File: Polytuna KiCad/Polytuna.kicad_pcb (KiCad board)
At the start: 2 copper layers, 114.3 x 64.8 mm, 47 parts, among them IC1 AP7313-33SAG-7, J1 Barrel_Jack, J2 Conn_01x02, J3 Conn_01x02, J4 Conn_01x04, J5 Conn_01x02, SW1 SW_Push, SW2 SW_Push, SW3 SW_Push, SW4 SW_TPDT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

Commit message: Added some logos
Still in need of tunas
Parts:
- G***: footprint uc3music_logos:logo_guitar_45x15.4mm -> uc3music_logos:logo_guitar_52.6.5x18.4mm
- moved G*** 4.35 mm to (156.5, 89.2)
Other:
- board text added: "Sergio Sánchez Rodríguez"

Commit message: Moar logos
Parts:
- moved J2 2.54 mm to (161.3, 142.2), turned to 270 degrees
- moved J3 2.54 mm to (174.2, 142.2), turned to 270 degrees
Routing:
- net GND: track 160.0 -> 193.4 mm
- net GNDA: track 39.2 -> 64.4 mm
- net Pin11_Teensy: track 11.4 -> 12.1 mm
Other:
- board text added: "Battery"

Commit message: Changed some logos. Added a tuna
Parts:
- removed the G*** at (218.8, 120.9)
- added G***: LOGO, uc3music_logos:logo_pick_10x10mm, F.Cu at (162.8, 111.8)
- added G***: LOGO, Silks Polytuna:tuna_fish_logo_21.7x21.7mm, F.Cu at (221.7, 120.1)

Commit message: MOAR TUNAS FOR EVERYBODY
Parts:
- added G***: LOGO, Silks Polytuna:tuna_fish_back1_L_54.2x27.1mm, B.Cu at (193.0, 71.1)
- added G***: LOGO, Silks Polytuna:tuna_fish_back3_R_8.1x8.1mm, B.Cu at (159.5, 102.6)
- added G***: LOGO, Silks Polytuna:tuna_fish_logo_10.8x10.8mm, B.Cu at (195.6, 126.0)
- added G***: LOGO, Silks Polytuna:tuna_fish_back3_L_19x9.5mm, B.Cu at (134.6, 103.4)
- added G***: LOGO, Silks Polytuna:tuna_fish_back1_L_25x12.5mm, B.Cu at (224.0, 129.0)
- added G***: LOGO, Silks Polytuna:tuna_fish_back2_R_16.4x16.4mm, B.Cu at (148.8, 133.1)
- added G***: LOGO, Silks Polytuna:tuna_fish_back3_R_15.5x7.7mm, B.Cu at (210.3, 117.1)
- added G***: LOGO, Silks Polytuna:tuna_fish_back1_L_8.1x4.1mm, F.Cu at (133.9, 136.9)
- moved Output1 0.80 mm to (193.3, 91.2)

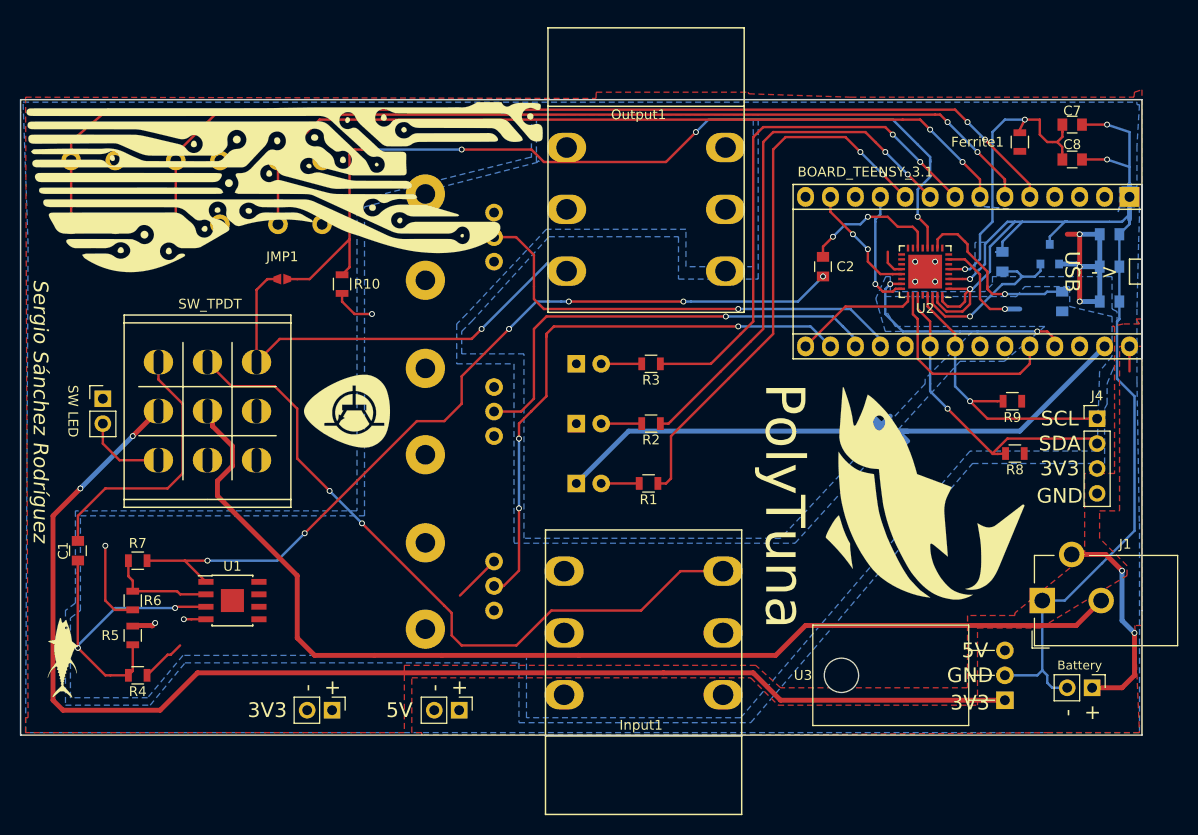
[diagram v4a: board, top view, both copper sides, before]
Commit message: Added some "Pibbles" and no DRC errors
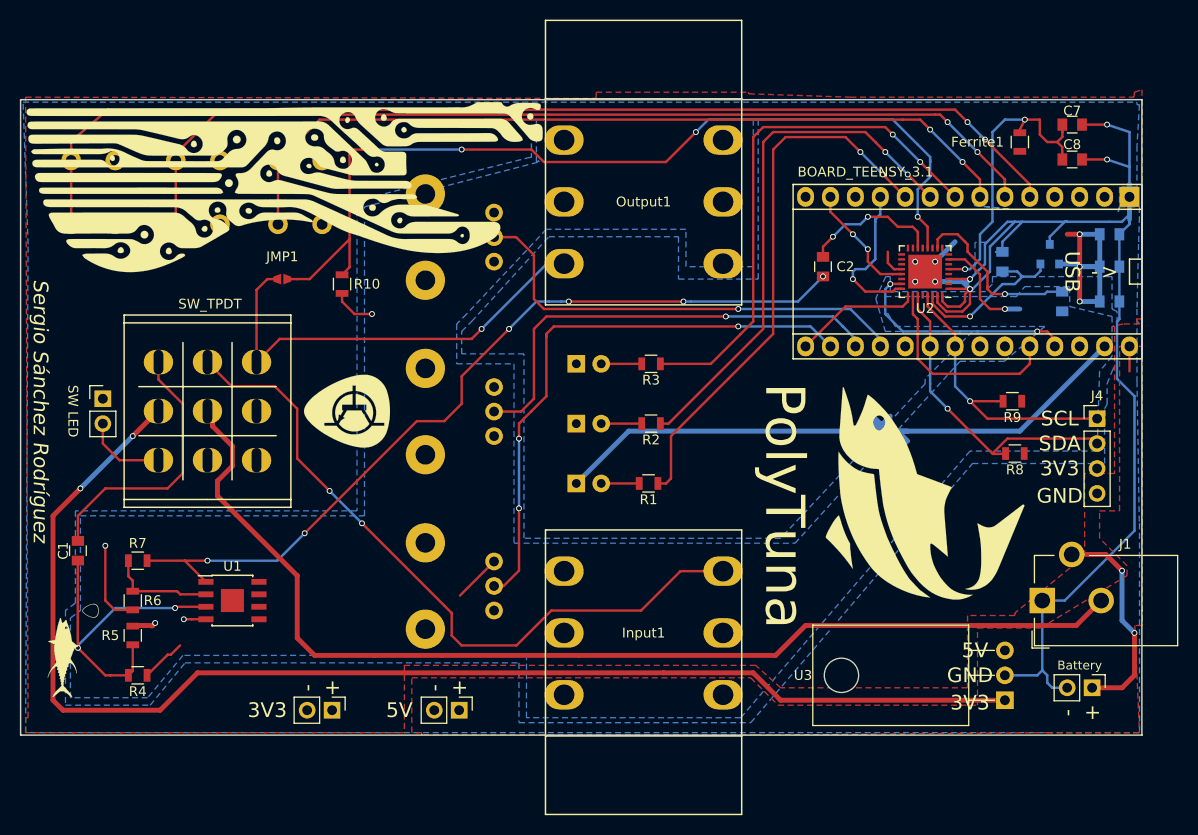
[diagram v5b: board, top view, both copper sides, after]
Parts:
- added G***: LOGO, Silks Polytuna:pick_contour_1.7mm, B.Cu at (135.6, 114.3)
- added G***: LOGO, Silks Polytuna:pick_contour_3mm, B.Cu at (141.2, 114.3)
- added G***: LOGO, Silks Polytuna:pick_contour_3mm, B.Cu at (152.4, 123.7)
- added G***: LOGO, Silks Polytuna:pick_contour_1.7mm, B.Cu at (157.5, 125.5)
- added G***: LOGO, Silks Polytuna:pick_contour_3.4mm, B.Cu at (197.9, 100.6)
- added G***: LOGO, Silks Polytuna:pick_contour_2.7mm, B.Cu at (205.5, 99.3)
- added G***: LOGO, Silks Polytuna:pick_contour_1.7mm, B.Cu at (210.1, 101.9)
- added G***: LOGO, Silks Polytuna:pick_contour_1.7mm, B.Cu at (162.3, 97.0)
- added G***: LOGO, Silks Polytuna:pick_contour_1.7mm, B.Cu at (195.3, 132.3)
- added G***: LOGO, Silks Polytuna:pick_contour_2.7mm, B.Cu at (200.2, 131.1)
- added G***: LOGO, Silks Polytuna:pick_contour_2.7mm, B.Cu at (213.9, 108.7)
- added G***: LOGO, Silks Polytuna:pick_contour_3.4mm, B.Cu at (232.7, 143.0)
- added G***: LOGO, Silks Polytuna:pick_contour_1.7mm, B.Cu at (223.5, 108.0)
- added G***: LOGO, Silks Polytuna:pick_contour_2.2mm, B.Cu at (219.2, 110.7)
- added G***: LOGO, Silks Polytuna:pick_contour_2.2mm, B.Cu at (162.1, 123.4)
- added G***: LOGO, Silks Polytuna:pick_contour_1.7mm, F.Cu at (136.7, 132.1)
- moved Output1 0.80 mm to (193.0, 90.4)
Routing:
- net GND: track 193.4 -> 203.8 mm
- net Pin9_Teensy: track 12.2 -> 15.7 mm

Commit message: PCB v1 finished
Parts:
- added G***: LOGO, Silks Polytuna:pick_contour_1.7mm, B.Cu at (227.1, 141.7)
- moved JMP2 0.25 mm to (217.9, 114.0), turned to 135 degrees
- renumbered D1 to LED1, D2 to LED2, D3 to LED3
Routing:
- net GNDA: track 64.4 -> 60.7 mm
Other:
- board text added: "A0"
- board text added: "A1"
- board text added: "A2"
- board text added: "D3"
- board text added: "D4"
- board text added: "D5"
- board text added: "D6"
- board text added: "D7"
- board text added: "D8"

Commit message: Some fixes
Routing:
- net GND: track 203.8 -> 209.7 mm
- net +3V3: track 50.2 -> 45.6 mm

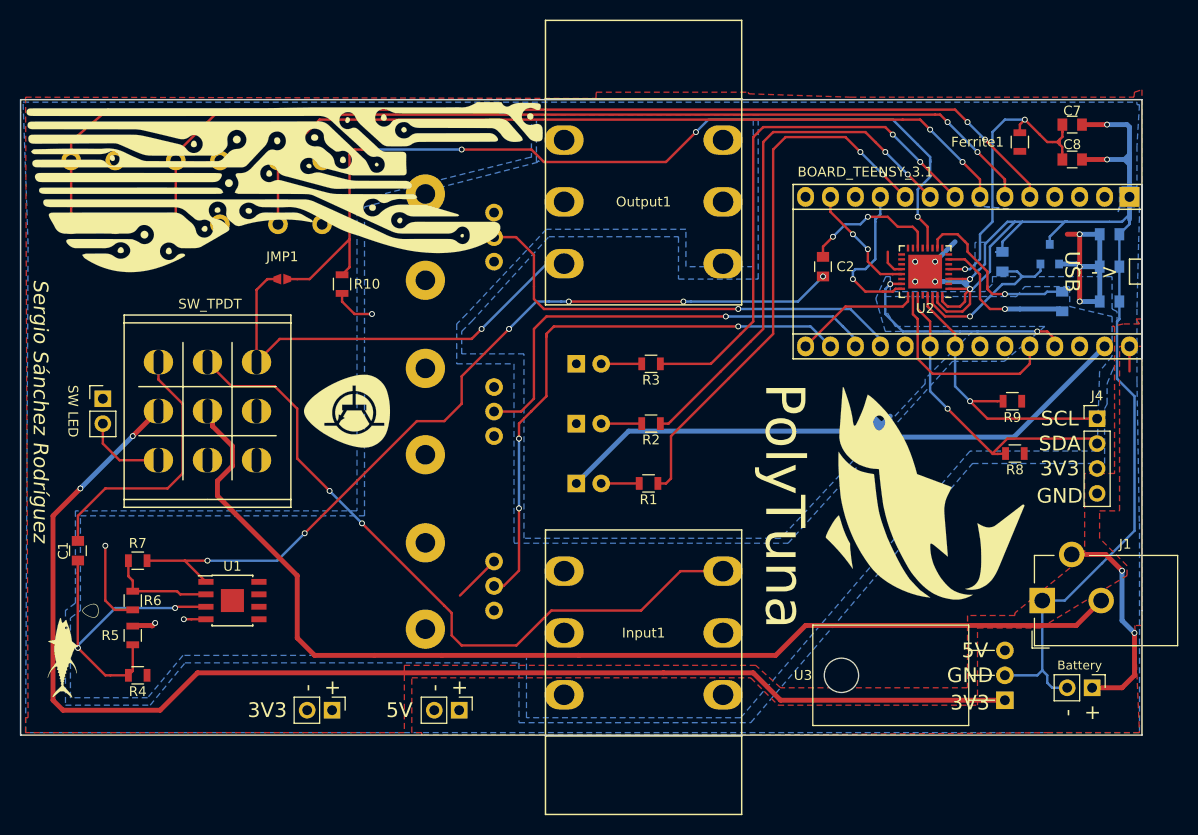
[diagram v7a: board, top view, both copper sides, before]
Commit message: Nice and round edges
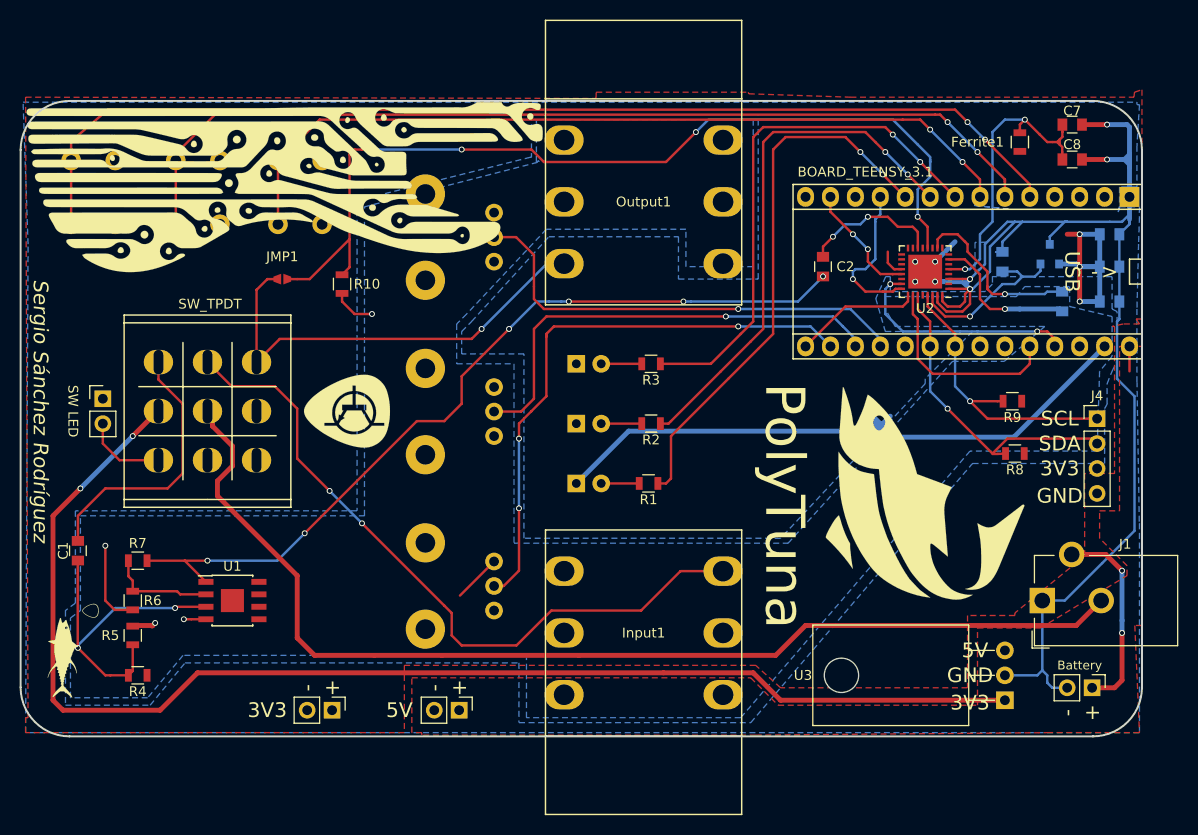
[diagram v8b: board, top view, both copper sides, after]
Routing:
- net Net-(BT1-Pad1): track 36.5 -> 28.9 mm
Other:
- outline, holes or cut-outs redrawn
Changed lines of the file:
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@@
     (links 120)
     (no_connects 0)
-    (area 129.464999 43.821666 258.608484 153.141001)
+    (area -57.250001 -32.485001 258.608484 153.141001)
     (thickness 1.6)
-    (drawings 42)
-    (tracks 594)
+    (drawings 44)
+    (tracks 592)
     (zones 0)
     (modules 73)
@@
     (effects (font (size 1.5 1.5) (thickness 0.3)))
   )
-  (gr_line (start 243.84 80.01) (end 243.84 132.08) (angle 90) (layer Edge.Cuts) (width 0.15))
-  (gr_line (start 129.54 80.01) (end 129.54 81.28) (angle 90) (layer Edge.Cuts) (width 0.15))
-  (gr_line (start 243.84 80.01) (end 129.54 80.01) (angle 90) (layer Edge.Cuts) (width 0.15))
-  (gr_line (start 243.84 144.78) (end 243.84 132.08) (angle 90) (layer Edge.Cuts) (width 0.15))
-  (gr_line (start 129.54 144.78) (end 243.84 144.78) (angle 90) (layer Edge.Cuts) (width 0.15))
-  (gr_line (start 129.54 81.28) (end 129.54 144.78) (angle 90) (layer Edge.Cuts) (width 0.15))
+  (gr_line (start 134.54 80.137) (end 238.84 80.137) (angle 90) (layer Edge.Cuts) (width 0.2))
+  (gr_line (start 243.84 85.137) (end 243.84 139.907) (angle 90) (layer Edge.Cuts) (width 0.2))
+  (gr_line (start 238.84 144.907) (end 134.54 144.907) (angle 90) (layer Edge.Cuts) (width 0.2))
+  (gr_line (start 129.54 139.907) (end 129.54 85.137) (angle 90) (layer Edge.Cuts) (width 0.2))
+  (gr_arc (start 238.84 85.137) (end 238.84 80.137) (angle 90) (layer Edge.Cuts) (width 0.2))
+  (gr_arc (start 238.84 139.907) (end 243.84 139.907) (angle 90) (layer Edge.Cuts) (width 0.2))
+  (gr_arc (start 134.54 139.907) (end 134.54 144.907) (angle 90) (layer Edge.Cuts) (width 0.2))
+  (gr_arc (start 134.54 85.137) (end 129.54 85.137) (angle 90) (layer Edge.Cuts) (width 0.2))
   (segment (start 240.284 82.55) (end 237.728 82.55) (width 0.5) (layer F.Cu) (net 1))
   (segment (start 240.284 86.106) (end 237.728 86.106) (width 0.5) (layer F.Cu) (net 1))
@@
   (segment (start 139.126 132.014) (end 138.176 131.064) (width 0.25) (layer F.Cu) (net 19))
   (segment (start 242.57 105.156) (end 242.57 107.696) (width 0.25) (layer F.Cu) (net 20))
+  (segment (start 241.808 134.366) (end 241.808 139.192) (width 0.5) (layer F.Cu) (net 21))
+  (segment (start 241.808 139.192) (end 241.046 139.954) (width 0.5) (layer F.Cu) (net 21))
   (segment (start 241.808 128.016) (end 240.156 126.364) (width 0.5) (layer F.Cu) (net 21))
   (segment (start 240.156 126.364) (end 236.68 126.364) (width 0.5) (layer F.Cu) (net 21))
-  (segment (start 243.078 134.366) (end 241.808 133.096) (width 0.5) (layer B.Cu) (net 21))
+  (segment (start 241.808 134.366) (end 241.808 133.096) (width 0.5) (layer B.Cu) (net 21))
   (segment (start 241.808 133.096) (end 241.808 128.016) (width 0.5) (layer B.Cu) (net 21))
-  (segment (start 238.76 139.954) (end 241.808 139.954) (width 0.5) (layer F.Cu) (net 21))
-  (segment (start 241.808 139.954) (end 243.078 138.684) (width 0.5) (layer F.Cu) (net 21))
-  (segment (start 243.078 138.684) (end 243.078 134.366) (width 0.5) (layer F.Cu) (net 21))
-  (segment (start 243.078 138.684) (end 243.078 134.366) (width 0.25) (layer F.Cu) (net 21))
-  (segment (start 241.808 139.954) (end 243.078 138.684) (width 0.25) (layer F.Cu) (net 21))
+  (segment (start 238.76 139.954) (end 241.046 139.954) (width 0.5) (layer F.Cu) (net 21))
   (segment (start 240.156 126.364) (end 236.68 126.364) (width 0.25) (layer F.Cu) (net 21))
-  (via (at 243.078 134.366) (size 0.6) (drill 0.4) (layers F.Cu B.Cu) (net 21))
+  (via (at 241.808 134.366) (size 0.6) (drill 0.4) (layers F.Cu B.Cu) (net 21))
   (segment (start 241.808 133.096) (end 241.808 128.016) (width 0.25) (layer B.Cu) (net 21))
   (via (at 241.808 128.016) (size 0.6) (drill 0.4) (layers F.Cu B.Cu) (net 21))
